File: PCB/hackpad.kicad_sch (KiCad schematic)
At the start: 9 parts, among them SW10 RotaryEncoder_Switch_MP, SW4 SW_Push, SW5 SW_Push, SW6 SW_Push, SW7 SW_Push, SW8 SW_Push, SW9 SW_Push, U1 XIAO-RP2040-DIP

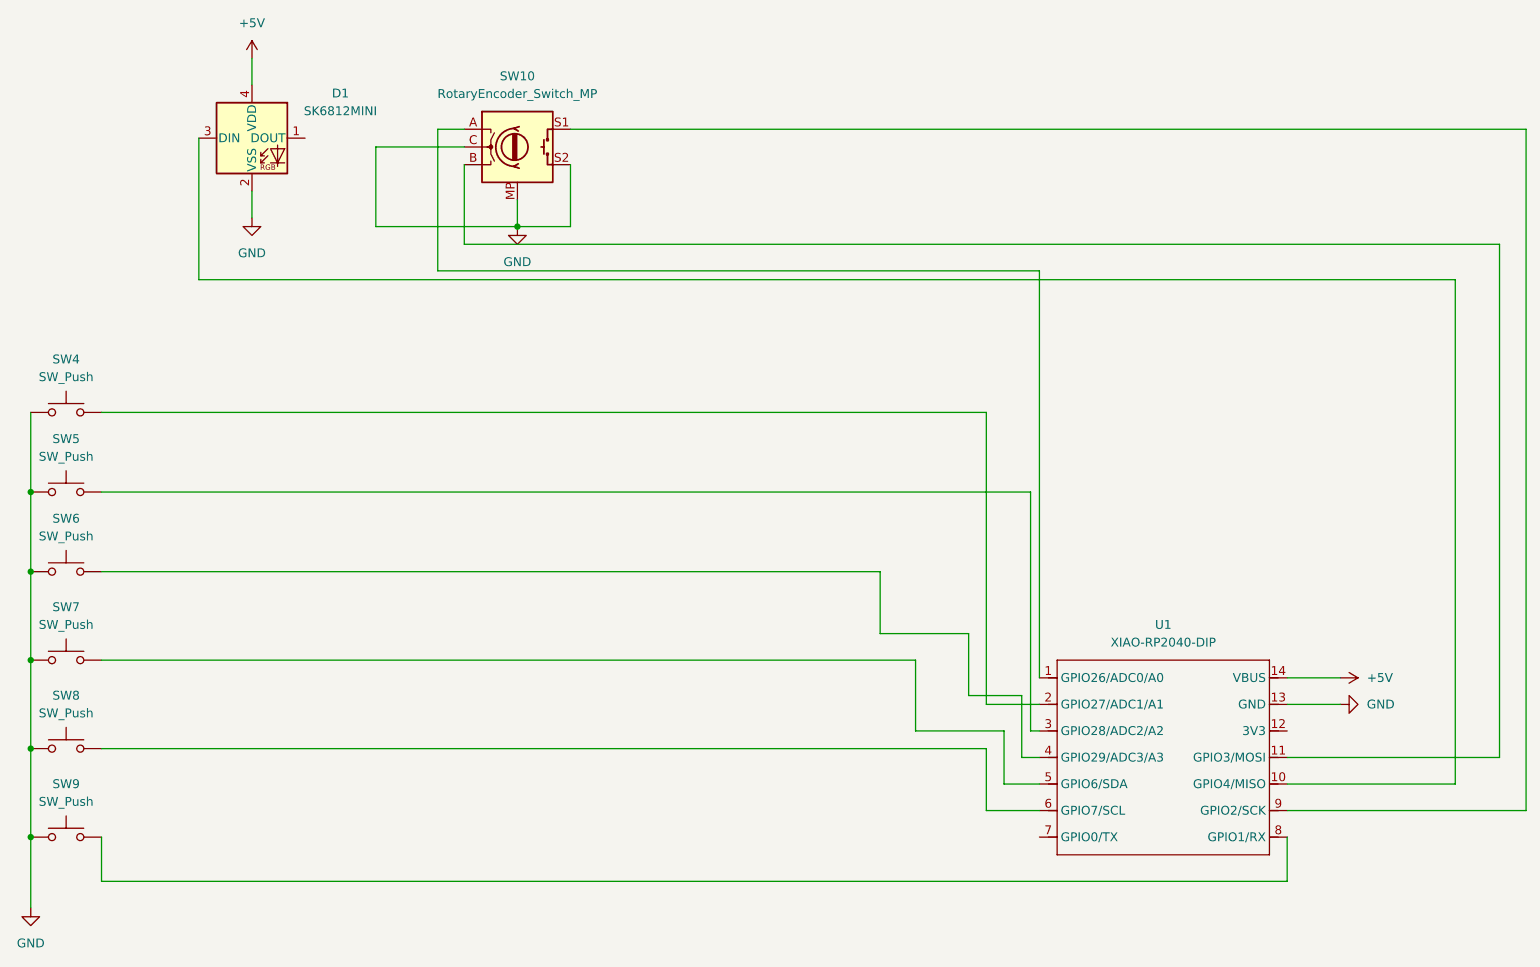
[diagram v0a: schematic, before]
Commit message: Changed Rotary Encoder from MP to non-MP
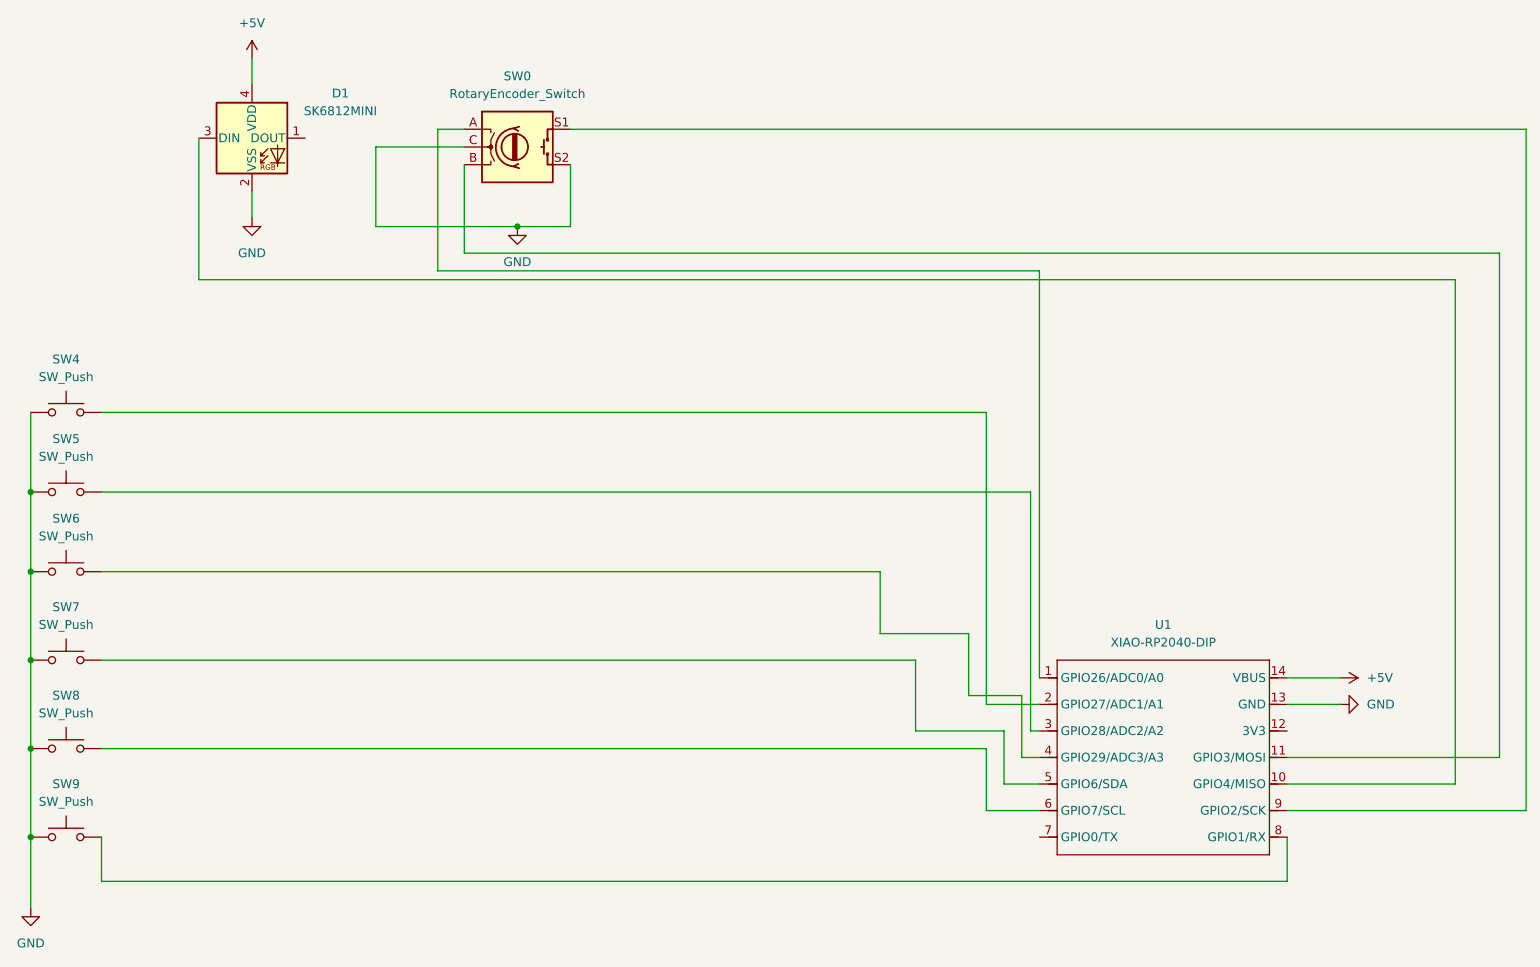
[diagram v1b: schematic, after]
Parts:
- SW0: renamed from SW10; value RotaryEncoder_Switch_MP -> RotaryEncoder_Switch; symbol Device:RotaryEncoder_Switch_MP -> Device:RotaryEncoder_Switch
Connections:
- net GND: no longer SW0.MP
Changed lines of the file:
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@@
-	(wire
-		(pts
-			(xy 92.71 38.1) (xy 92.71 41.91)
-		)
-		(stroke
-			(width 0)
-			(type default)
-		)
-	)
 	(wire
 		(pts
@@
 	(wire
 		(pts
-			(xy 233.68 44.45) (xy 233.68 118.11)
+			(xy 233.68 45.72) (xy 233.68 118.11)
 		)
 		(stroke
@@
 	(wire
 		(pts
-			(xy 85.09 44.45) (xy 233.68 44.45)
+			(xy 85.09 45.72) (xy 233.68 45.72)
 		)
 		(stroke
@@
 	(wire
 		(pts
-			(xy 85.09 33.02) (xy 85.09 44.45)
+			(xy 85.09 33.02) (xy 85.09 45.72)
 		)
 		(stroke
@@
 	)
 	(symbol
-		(lib_id "Device:RotaryEncoder_Switch_MP")
+		(lib_id "Device:RotaryEncoder_Switch")
 		(at 92.71 30.48 0)
 		(unit 1)
@@
 		(dnp no)
 		(fields_autoplaced yes)
-		(property "Reference" "SW10"
+		(property "Reference" "SW0"
 			(at 92.71 20.32 0)
 			(effects
@@
 			)
 		)
-		(property "Value" "RotaryEncoder_Switch_MP"
+		(property "Value" "RotaryEncoder_Switch"
 			(at 92.71 22.86 0)
 			(effects
@@
 		)
 		(property "Datasheet" "~"
-			(at 92.71 43.18 0)
-			(effects
-				(font
-					(size 1.27 1.27)
-				)
-				(hide yes)
-			)
-		)
-		(property "Description" "Rotary encoder, dual channel, incremental quadrate outputs, with switch and MP Pin"
-			(at 92.71 45.72 0)
+			(at 92.71 23.876 0)
+			(effects
+				(font
+					(size 1.27 1.27)
+				)
+				(hide yes)
+			)
+		)
+		(property "Description" "Rotary encoder, dual channel, incremental quadrate outputs, with switch"
+			(at 92.71 30.48 0)
 			(effects
 				(font
@@
 		)
 		(pin "B"
-		)
-		(pin "MP"
 		)
 		(pin "S1"
@@
 			(project ""
 				(path "/64efc079-13c1-405f-8e4e-7d1237ab7ef2"
-					(reference "SW10")
+					(reference "SW0")
 					(unit 1)
 				)
